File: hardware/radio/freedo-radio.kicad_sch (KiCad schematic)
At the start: 0 parts

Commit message: feat(hardware): draw the rev a schematic
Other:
- added sheet ethernet_poe (ethernet_poe.kicad_sch)
- added sheet mcu (mcu.kicad_sch)
- added sheet rf (rf.kicad_sch)
- added sheet usb_power (usb_power.kicad_sch)
- note added: "5V_SYS: diode-OR of USB (D202) and PoE (D402)"
- note added: "J201 USB-C, F201 PTC D201 TVS, U202 ESD D202 USB OR diode U203 LDO 3V3"
- note added: "U1 CC1101, X1 26 MHz TI EM 868 MHz match J1 SMA (hand)"
- note added: "U201 ESP32-S3-MINI-1-N8 SW201 RESET, SW202 BOOT D203-D206 LEDs J202 UART0 (DNP)"
- note added: "U301 W5500, T301 B1608S J301 RJ45 (hand) U401 PoE module (opt) D402 PoE OR diode"
- title: (none) -> freedo radio rev A

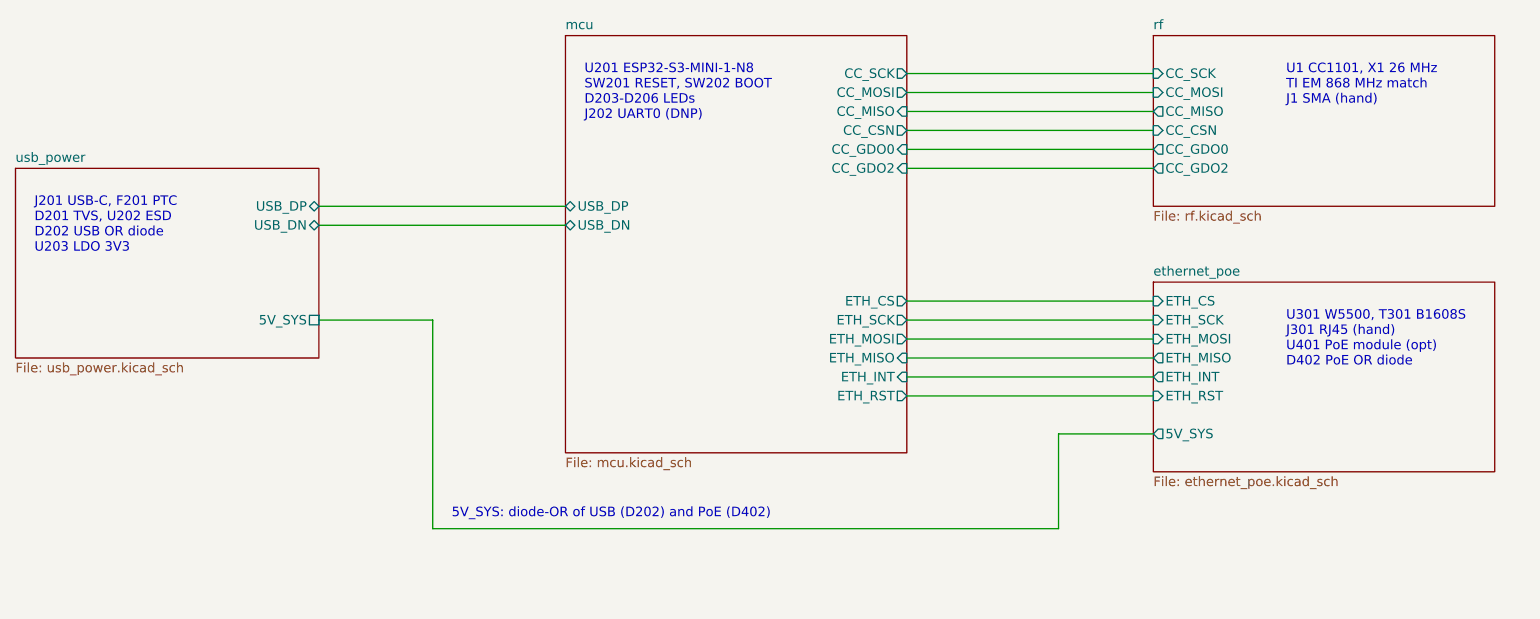
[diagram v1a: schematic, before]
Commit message: feat(hardware): move the radio to the ebyte e07 module and fix the power review findings
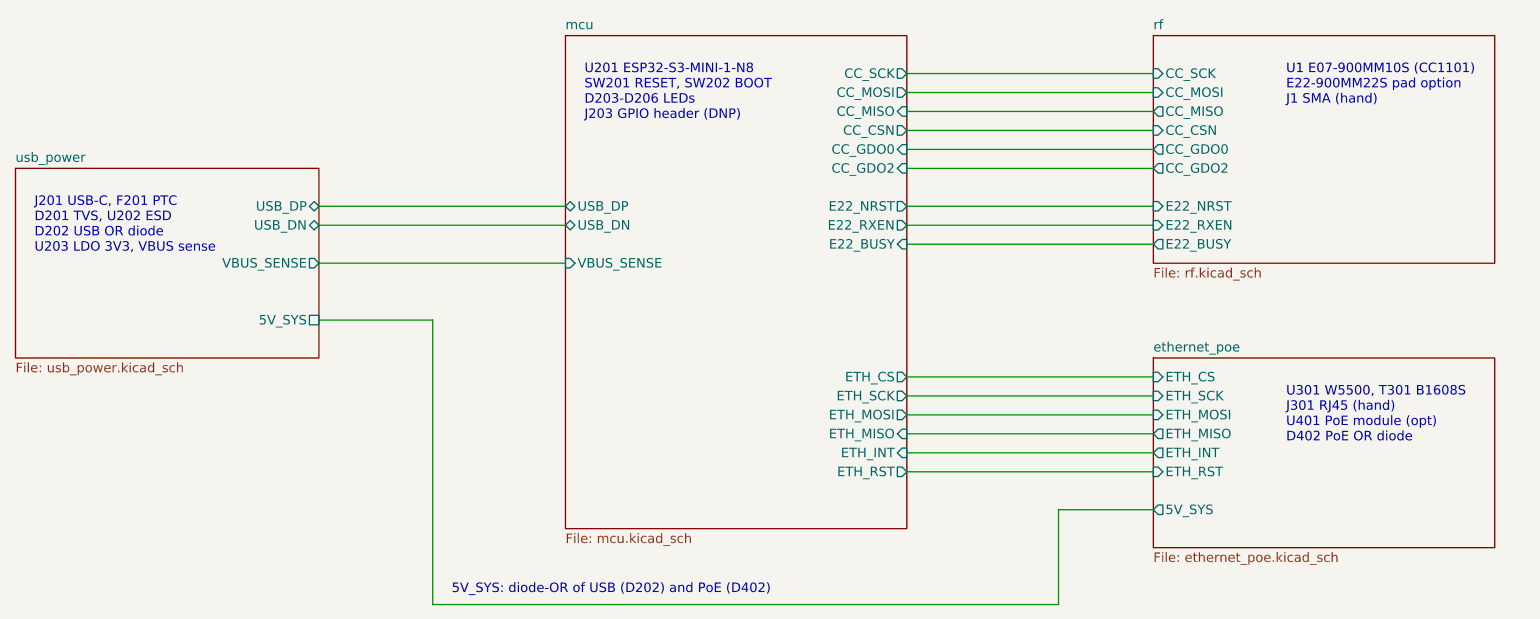
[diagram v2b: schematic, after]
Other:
- sheet mcu ports: added E22_BUSY, E22_NRST, E22_RXEN, VBUS_SENSE; removed none
- sheet rf ports: added E22_BUSY, E22_NRST, E22_RXEN; removed none
- sheet usb_power ports: added VBUS_SENSE; removed none
- note added: "J201 USB-C, F201 PTC D201 TVS, U202 ESD D202 USB OR diode U203 LDO 3V3, VBUS sense"
- note added: "U1 E07-900MM10S (CC1101) E22-900MM22S pad option J1 SMA (hand)"
- note added: "U201 ESP32-S3-MINI-1-N8 SW201 RESET, SW202 BOOT D203-D206 LEDs J203 GPIO header (DNP)"
- note removed: "J201 USB-C, F201 PTC D201 TVS, U202 ESD D202 USB OR diode U203 LDO 3V3"
- note removed: "U1 CC1101, X1 26 MHz TI EM 868 MHz match J1 SMA (hand)"
- note removed: "U201 ESP32-S3-MINI-1-N8 SW201 RESET, SW202 BOOT D203-D206 LEDs J202 UART0 (DNP)"
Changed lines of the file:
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@@
 		(date "2026-09-24")
 		(rev "A")
-		(comment 1 "ESP32-S3-MINI-1-N8, CC1101 868 MHz, W5500 Ethernet, optional isolated PoE, USB-C")
+		(comment 1 "ESP32-S3-MINI-1-N8, E07-900MM10S 868 MHz, W5500 Ethernet, isolated PoE option, USB-C")
 		(comment 2 "Design spec: hardware/radio/README.md")
 	)
@@
 	(wire
 		(pts
-			(xy 165.1 86.36)
-			(xy 198.12 86.36)
-		)
-	)
-	(wire
-		(pts
-			(xy 165.1 88.9)
-			(xy 198.12 88.9)
-		)
-	)
-	(wire
-		(pts
-			(xy 165.1 91.44)
-			(xy 198.12 91.44)
-		)
-	)
-	(wire
-		(pts
-			(xy 165.1 93.98)
-			(xy 198.12 93.98)
-		)
-	)
-	(wire
-		(pts
 			(xy 165.1 96.52)
 			(xy 198.12 96.52)
@@
 	(wire
 		(pts
+			(xy 165.1 101.6)
+			(xy 198.12 101.6)
+		)
+	)
+	(wire
+		(pts
+			(xy 165.1 104.14)
+			(xy 198.12 104.14)
+		)
+	)
+	(wire
+		(pts
+			(xy 165.1 106.68)
+			(xy 198.12 106.68)
+		)
+	)
+	(wire
+		(pts
+			(xy 165.1 109.22)
+			(xy 198.12 109.22)
+		)
+	)
+	(wire
+		(pts
 			(xy 86.36 88.9)
 			(xy 101.6 88.9)
@@
 		(pts
 			(xy 101.6 88.9)
-			(xy 101.6 116.84)
-		)
-	)
-	(wire
-		(pts
-			(xy 101.6 116.84)
-			(xy 185.42 116.84)
-		)
-	)
-	(wire
-		(pts
-			(xy 185.42 116.84)
-			(xy 185.42 104.14)
-		)
-	)
-	(wire
-		(pts
-			(xy 185.42 104.14)
-			(xy 198.12 104.14)
+			(xy 101.6 127)
+		)
+	)
+	(wire
+		(pts
+			(xy 101.6 127)
+			(xy 185.42 127)
+		)
+	)
+	(wire
+		(pts
+			(xy 185.42 127)
+			(xy 185.42 114.3)
+		)
+	)
+	(wire
+		(pts
+			(xy 185.42 114.3)
+			(xy 198.12 114.3)
+		)
+	)
+	(wire
+		(pts
+			(xy 86.36 81.28)
+			(xy 119.38 81.28)
+		)
+		(stroke
+			(width 0)
+			(type default)
+		)
+	)
+	(wire
+		(pts
+			(xy 165.1 73.66)
+			(xy 198.12 73.66)
+		)
+		(stroke
+			(width 0)
+			(type default)
+		)
+	)
+	(wire
+		(pts
+			(xy 165.1 76.2)
+			(xy 198.12 76.2)
+		)
+		(stroke
+			(width 0)
+			(type default)
+		)
+	)
+	(wire
+		(pts
+			(xy 165.1 78.74)
+			(xy 198.12 78.74)
+		)
+		(stroke
+			(width 0)
+			(type default)
 		)
 	)
@@
 			)
 		)
+		(pin "VBUS_SENSE" output
+			(at 86.36 81.28 0)
+			(effects
+				(font
+					(size 1.27 1.27)
+				)
+				(justify right)
+			)
+		)
 		(instances
 			(project "freedo-radio"
@@
 	(sheet
 		(at 119.38 50.8)
-		(size 45.72 55.88)
+		(size 45.72 66.04)
 		(fields_autoplaced)
 		(exclude_from_sim no)
@@
 		)
 		(property "Sheetfile" "mcu.kicad_sch"
-			(at 119.38 107.2646 0)
+			(at 119.38 117.4246 0)
 			(effects
 				(font
@@
 		)
 		(pin "ETH_RST" output
+			(at 165.1 109.22 0)
+			(effects
+				(font
+					(size 1.27 1.27)
+				)
+				(justify right)
+			)
+		)
+		(pin "ETH_CS" output
+			(at 165.1 96.52 0)
+			(effects
+				(font
+					(size 1.27 1.27)
+				)
+				(justify right)
+			)
+		)
+		(pin "ETH_MOSI" output
+			(at 165.1 101.6 0)
+			(effects
+				(font
+					(size 1.27 1.27)
+				)
+				(justify right)
+			)
+		)
+		(pin "ETH_SCK" output
 			(at 165.1 99.06 0)
 			(effects
@@
 			)
 		)
-		(pin "ETH_CS" output
-			(at 165.1 86.36 0)
-			(effects
-				(font
-					(size 1.27 1.27)
-				)
-				(justify right)
-			)
-		)
-		(pin "ETH_MOSI" output
-			(at 165.1 91.44 0)
-			(effects
-				(font
-					(size 1.27 1.27)
-				)
-				(justify right)
-			)
-		)
-		(pin "ETH_SCK" output
-			(at 165.1 88.9 0)
-			(effects
-				(font
-					(size 1.27 1.27)
-				)
-				(justify right)
-			)
-		)
 		(pin "ETH_MISO" input
-			(at 165.1 93.98 0)
+			(at 165.1 104.14 0)
 			(effects
 				(font
@@
 		)
 		(pin "ETH_INT" input
-			(at 165.1 96.52 0)
+			(at 165.1 106.68 0)
 			(effects
 				(font
@@
 		(pin "USB_DP" bidirectional
 			(at 119.38 73.66 180)
+			(effects
+				(font
+					(size 1.27 1.27)
+				)
+				(justify left)
+			)
+		)
+		(pin "E22_NRST" output
+			(at 165.1 73.66 0)
+			(effects
+				(font
+					(size 1.27 1.27)
+				)
+				(justify right)
+			)
+		)
+		(pin "E22_RXEN" output
+			(at 165.1 76.2 0)
+			(effects
+				(font
+					(size 1.27 1.27)
+				)
+				(justify right)
+			)
+		)
+		(pin "E22_BUSY" input
+			(at 165.1 78.74 0)
+			(effects
+				(font
+					(size 1.27 1.27)
+				)
+				(justify right)
+			)
+		)
+		(pin "VBUS_SENSE" input
+			(at 119.38 81.28 180)
 			(effects
 				(font
@@
 	(sheet
 		(at 198.12 50.8)
-		(size 45.72 22.86)
+		(size 45.72 30.48)
 		(fields_autoplaced)
 		(exclude_from_sim no)
@@
 		)
 		(property "Sheetfile" "rf.kicad_sch"
-			(at 198.12 74.2446 0)
+			(at 198.12 81.8646 0)
 			(effects
 				(font
@@
 		(pin "CC_GDO2" output
 			(at 198.12 68.58 180)
+			(effects
+				(font
+					(size 1.27 1.27)
+				)
+				(justify left)
+			)
+		)
+		(pin "E22_NRST" input
+			(at 198.12 73.66 180)
+			(effects
+				(font
+					(size 1.27 1.27)
+				)
+				(justify left)
+			)
+		)
+		(pin "E22_RXEN" input
+			(at 198.12 76.2 180)
+			(effects
+				(font
+					(size 1.27 1.27)
+				)
+				(justify left)
+			)
+		)
+		(pin "E22_BUSY" output
+			(at 198.12 78.74 180)
 			(effects
 				(font
@@
 	)
 	(sheet
-		(at 198.12 83.82)
+		(at 198.12 93.98)
 		(size 45.72 25.4)
 		(fields_autoplaced)
@@
 		)
 		(property "Sheetname" "ethernet_poe"
-			(at 198.12 83.1084 0)
+			(at 198.12 93.2684 0)
 			(effects
 				(font
@@
 		)
 		(property "Sheetfile" "ethernet_poe.kicad_sch"
-			(at 198.12 109.8046 0)
+			(at 198.12 119.9646 0)
 			(effects
 				(font
@@
 		)
 		(pin "5V_SYS" output
+			(at 198.12 114.3 180)
+			(effects
+				(font
+					(size 1.27 1.27)
+				)
+				(justify left)
+			)
+		)
+		(pin "ETH_CS" input
+			(at 198.12 96.52 180)
+			(effects
+				(font
+					(size 1.27 1.27)
+				)
+				(justify left)
+			)
+		)
+		(pin "ETH_SCK" input
+			(at 198.12 99.06 180)
+			(effects
+				(font
+					(size 1.27 1.27)
+				)
+				(justify left)
+			)
+		)
+		(pin "ETH_MOSI" input
+			(at 198.12 101.6 180)
+			(effects
+				(font
+					(size 1.27 1.27)
+				)
+				(justify left)
+			)
+		)
+		(pin "ETH_MISO" output
 			(at 198.12 104.14 180)
 			(effects
@@
 			)
 		)
-		(pin "ETH_CS" input
-			(at 198.12 86.36 180)
-			(effects
-				(font
-					(size 1.27 1.27)
-				)
-				(justify left)
-			)
-		)
-		(pin "ETH_SCK" input
-			(at 198.12 88.9 180)
-			(effects
-				(font
-					(size 1.27 1.27)
-				)
-				(justify left)
-			)
-		)
-		(pin "ETH_MOSI" input
-			(at 198.12 91.44 180)
-			(effects
-				(font
-					(size 1.27 1.27)
-				)
-				(justify left)
-			)
-		)
-		(pin "ETH_MISO" output
-			(at 198.12 93.98 180)
-			(effects
-				(font
-					(size 1.27 1.27)
-				)
-				(justify left)
-			)
-		)
 		(pin "ETH_INT" output
-			(at 198.12 96.52 180)
+			(at 198.12 106.68 180)
 			(effects
 				(font
@@
 		)
 		(pin "ETH_RST" input
-			(at 198.12 99.06 180)
+			(at 198.12 109.22 180)
 			(effects
 				(font
@@
 		)
 	)
-  (text "J201 USB-C, F201 PTC\nD201 TVS, U202 ESD\nD202 USB OR diode\nU203 LDO 3V3"
+  (text "J201 USB-C, F201 PTC\nD201 TVS, U202 ESD\nD202 USB OR diode\nU203 LDO 3V3, VBUS sense"
     (at 48.26 72.39 0)
     (effects (font (size 1.27 1.27)) (justify left top))
   )
-  (text "U201 ESP32-S3-MINI-1-N8\nSW201 RESET, SW202 BOOT\nD203-D206 LEDs\nJ202 UART0 (DNP)"
+  (text "U201 ESP32-S3-MINI-1-N8\nSW201 RESET, SW202 BOOT\nD203-D206 LEDs\nJ203 GPIO header (DNP)"
     (at 121.92 54.61 0)
     (effects (font (size 1.27 1.27)) (justify left top))
   )
-  (text "U1 CC1101, X1 26 MHz\nTI EM 868 MHz match\nJ1 SMA (hand)"
+  (text "U1 E07-900MM10S (CC1101)\nE22-900MM22S pad option\nJ1 SMA (hand)"
     (at 215.9 54.61 0)
     (effects (font (size 1.27 1.27)) (justify left top))
   )
   (text "U301 W5500, T301 B1608S\nJ301 RJ45 (hand)\nU401 PoE module (opt)\nD402 PoE OR diode"
-    (at 215.9 87.63 0)
+    (at 215.9 97.79 0)
     (effects (font (size 1.27 1.27)) (justify left top))
   )
   (text "5V_SYS: diode-OR of USB (D202) and PoE (D402)"
-    (at 104.14 115.57 0)
+    (at 104.14 125.73 0)
     (effects (font (size 1.27 1.27)) (justify left bottom))
   )
